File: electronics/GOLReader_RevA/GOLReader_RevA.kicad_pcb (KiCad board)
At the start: 2 copper layers, 16 x 60 mm, 21 parts, among them P1 CONN_01X04, U1 TCRT5000, U2 TCRT5000, U3 LM393

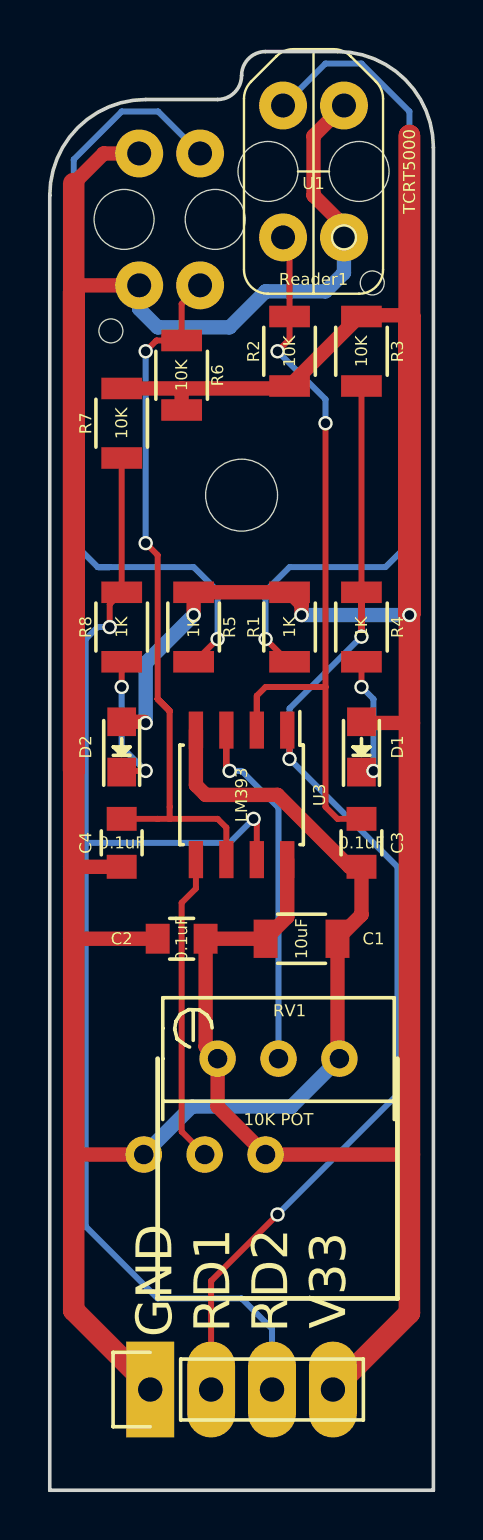
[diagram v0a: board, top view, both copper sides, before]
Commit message: added panelization of 12 units of the GOLReader, to cut pcb fabrication cost in half
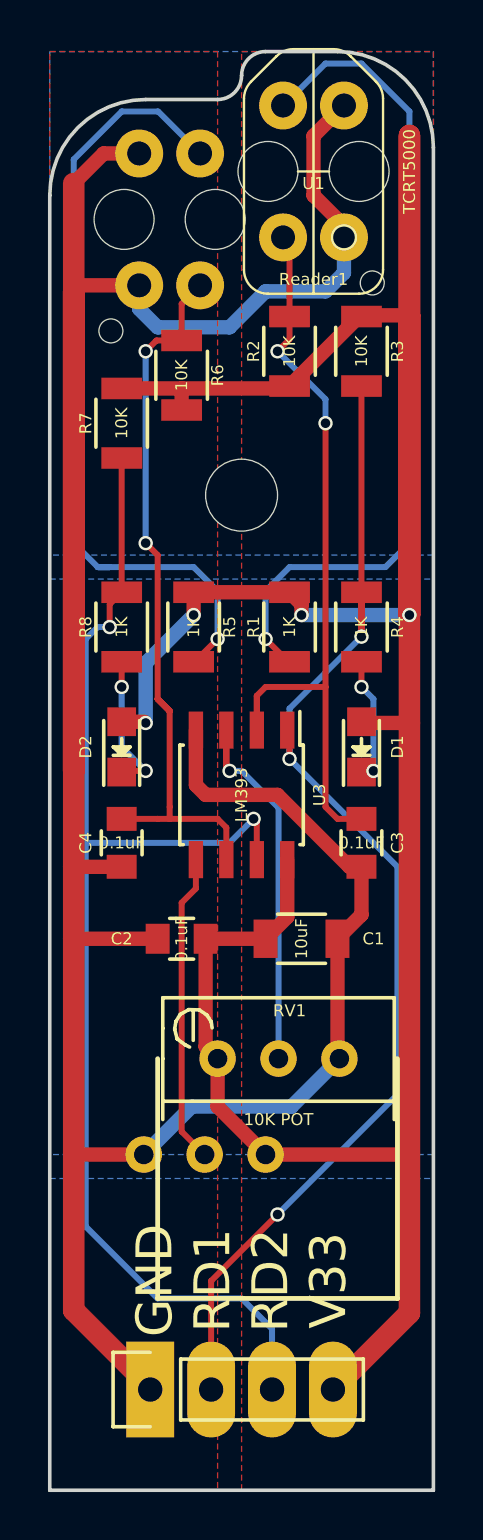
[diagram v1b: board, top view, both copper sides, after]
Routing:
- added copper zone on B.Cu, net GND
- added copper zone on F.Cu, net GND
- added copper zone on B.Cu, net V33
- added copper zone on F.Cu, net V33
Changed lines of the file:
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@@
     (links 42)
     (no_connects 0)
-    (area 66.899999 66.899999 188.100001 182.833333)
+    (area 118.924999 121.924999 151.075001 182.075001)
     (thickness 1.6)
     (drawings 24)
@@
     (user_trace_width 0.9)
     (trace_clearance 0.2)
-    (zone_clearance 0.508)
+    (zone_clearance 1)
     (zone_45_only no)
     (trace_min 0.2)
@@
     (pad 1 thru_hole circle (at 0 0) (size 3 3) (drill 3) (layers))
   )
+  (gr_line (start 135 126) (end 135 182) (angle 90) (layer Edge.Cuts) (width 0.15))
   (gr_line (start 127 127) (end 67 127) (angle 90) (layer Cmts.User) (width 0.2))
   (gr_line (start 127 127) (end 188 127) (angle 90) (layer Cmts.User) (width 0.2))
   (gr_line (start 127 127) (end 127 67) (angle 90) (layer Cmts.User) (width 0.2))
-  (gr_line (start 135 126) (end 135 182) (angle 90) (layer Edge.Cuts) (width 0.15))
   (gr_text Reader2 (at 124 133.5) (layer B.SilkS)
     (effects (font (size 0.5 0.5) (thickness 0.1)) (justify mirror))
@@
   (segment (start 124.5 157.5) (end 125.095 156.905) (width 0.25) (layer F.Cu) (net 12))
   (segment (start 124.5 167.04) (end 124.5 157.5) (width 0.25) (layer F.Cu) (net 12))
+  (zone (net 2) (net_name GND) (layer F.Cu) (hatch edge 0.508)
+    (connect_pads (clearance 1))
+    (min_thickness 0.254)
+    (fill yes (arc_segments 16) (thermal_gap 1) (thermal_bridge_width 1))
+    (polygon
+      (pts
+        (xy 126 182) (xy 119 182) (xy 119 122) (xy 126 122)
+      )
+    )
+  )
+  (zone (net 1) (net_name V33) (layer F.Cu) (hatch edge 0.508)
+    (connect_pads (clearance 1))
+    (min_thickness 0.254)
+    (fill yes (arc_segments 16) (thermal_gap 1) (thermal_bridge_width 1))
+    (polygon
+      (pts
+        (xy 135 182) (xy 127 182) (xy 127 122) (xy 135 122)
+      )
+    )
+  )
+  (zone (net 1) (net_name V33) (layer B.Cu) (hatch edge 0.508)
+    (connect_pads (clearance 1))
+    (min_thickness 0.254)
+    (fill yes (arc_segments 16) (thermal_gap 1) (thermal_bridge_width 1))
+    (polygon
+      (pts
+        (xy 135 168) (xy 119 168) (xy 119 144) (xy 135 144)
+      )
+    )
+  )
+  (zone (net 2) (net_name GND) (layer B.Cu) (hatch edge 0.508)
+    (connect_pads (clearance 1))
+    (min_thickness 0.254)
+    (fill yes (arc_segments 16) (thermal_gap 1) (thermal_bridge_width 1))
+    (polygon
+      (pts
+        (xy 135 182) (xy 119 182) (xy 119 169) (xy 135 169)
+      )
+    )
+  )
+  (zone (net 2) (net_name GND) (layer B.Cu) (hatch edge 0.508)
+    (connect_pads (clearance 1))
+    (min_thickness 0.254)
+    (fill yes (arc_segments 16) (thermal_gap 1) (thermal_bridge_width 1))
+    (polygon
+      (pts
+        (xy 135 143) (xy 119 143) (xy 119 122) (xy 135 122)
+      )
+    )
+  )
 )
